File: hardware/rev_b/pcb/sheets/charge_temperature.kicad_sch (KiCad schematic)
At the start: 9 parts, among them Q2 2N7002P, U7 TLV9022DGK

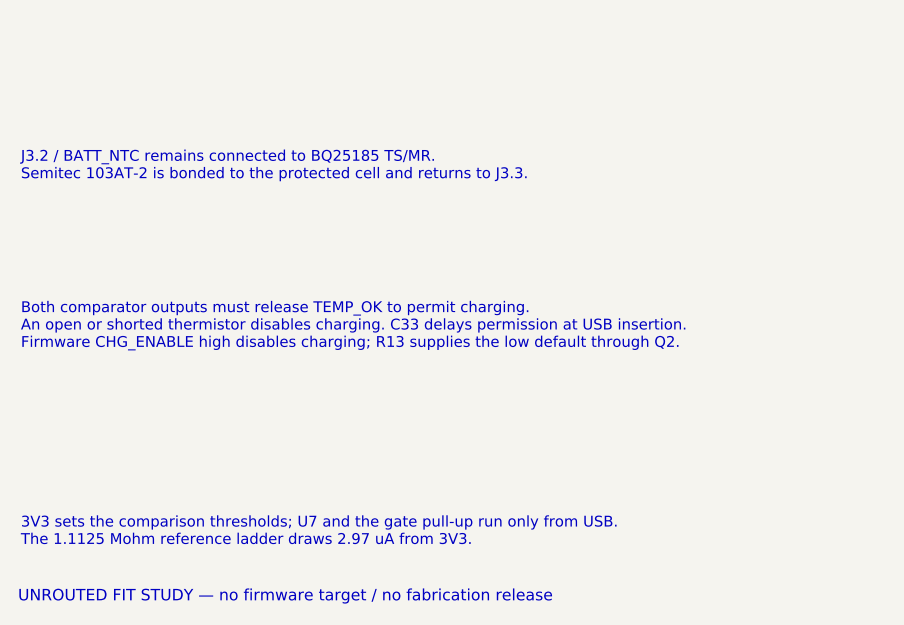
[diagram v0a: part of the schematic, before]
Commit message: fix(hw): recess Rev B controls and prepare first-article files
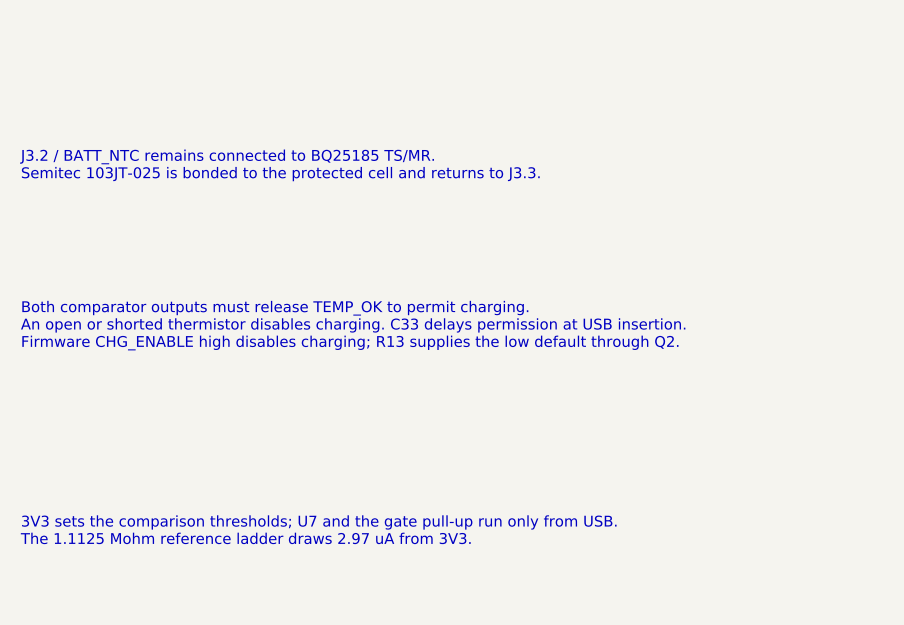
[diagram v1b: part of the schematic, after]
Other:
- note added: "J3.2 / BATT_NTC remains connected to BQ25185 TS/MR. Semitec 103JT-025 is bonded to the protected cell and returns to J3.3."
- note removed: "J3.2 / BATT_NTC remains connected to BQ25185 TS/MR. Semitec 103AT-2 is bonded to the protected cell and returns to J3.3."
- note removed: "UNROUTED FIT STUDY — no firmware target / no fabrication release"
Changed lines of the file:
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@@
 	(title_block
 		(title "Hardware charge temperature guard")
-		(date "2026-09-07")
-		(rev "Rev B FIT - NOT FOR FABRICATION")
+		(date "2026-09-16")
+		(rev "B.05")
 		(company "Cicala")
+		(comment 1 "Engineering prototype; physical qualification pending")
 	)
 	(symbol
@@
 		)
 	)
-	(text "J3.2 / BATT_NTC remains connected to BQ25185 TS/MR.\nSemitec 103AT-2 is bonded to the protected cell and returns to J3.3."
+	(text "J3.2 / BATT_NTC remains connected to BQ25185 TS/MR.\nSemitec 103JT-025 is bonded to the protected cell and returns to J3.3."
 		(at 20.32 137.16 0)
 		(effects
@@
 	)
 	(embedded_fonts no)
-	(text "UNROUTED FIT STUDY — no firmware target / no fabrication release"
-		(at 20 185 0)
-		(effects
-			(font
-				(size 1.27 1.27)
-			)
-			(justify left)
-		)
-	)
 )
